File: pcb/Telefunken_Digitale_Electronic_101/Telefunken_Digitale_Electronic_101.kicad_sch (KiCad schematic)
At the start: 0 parts

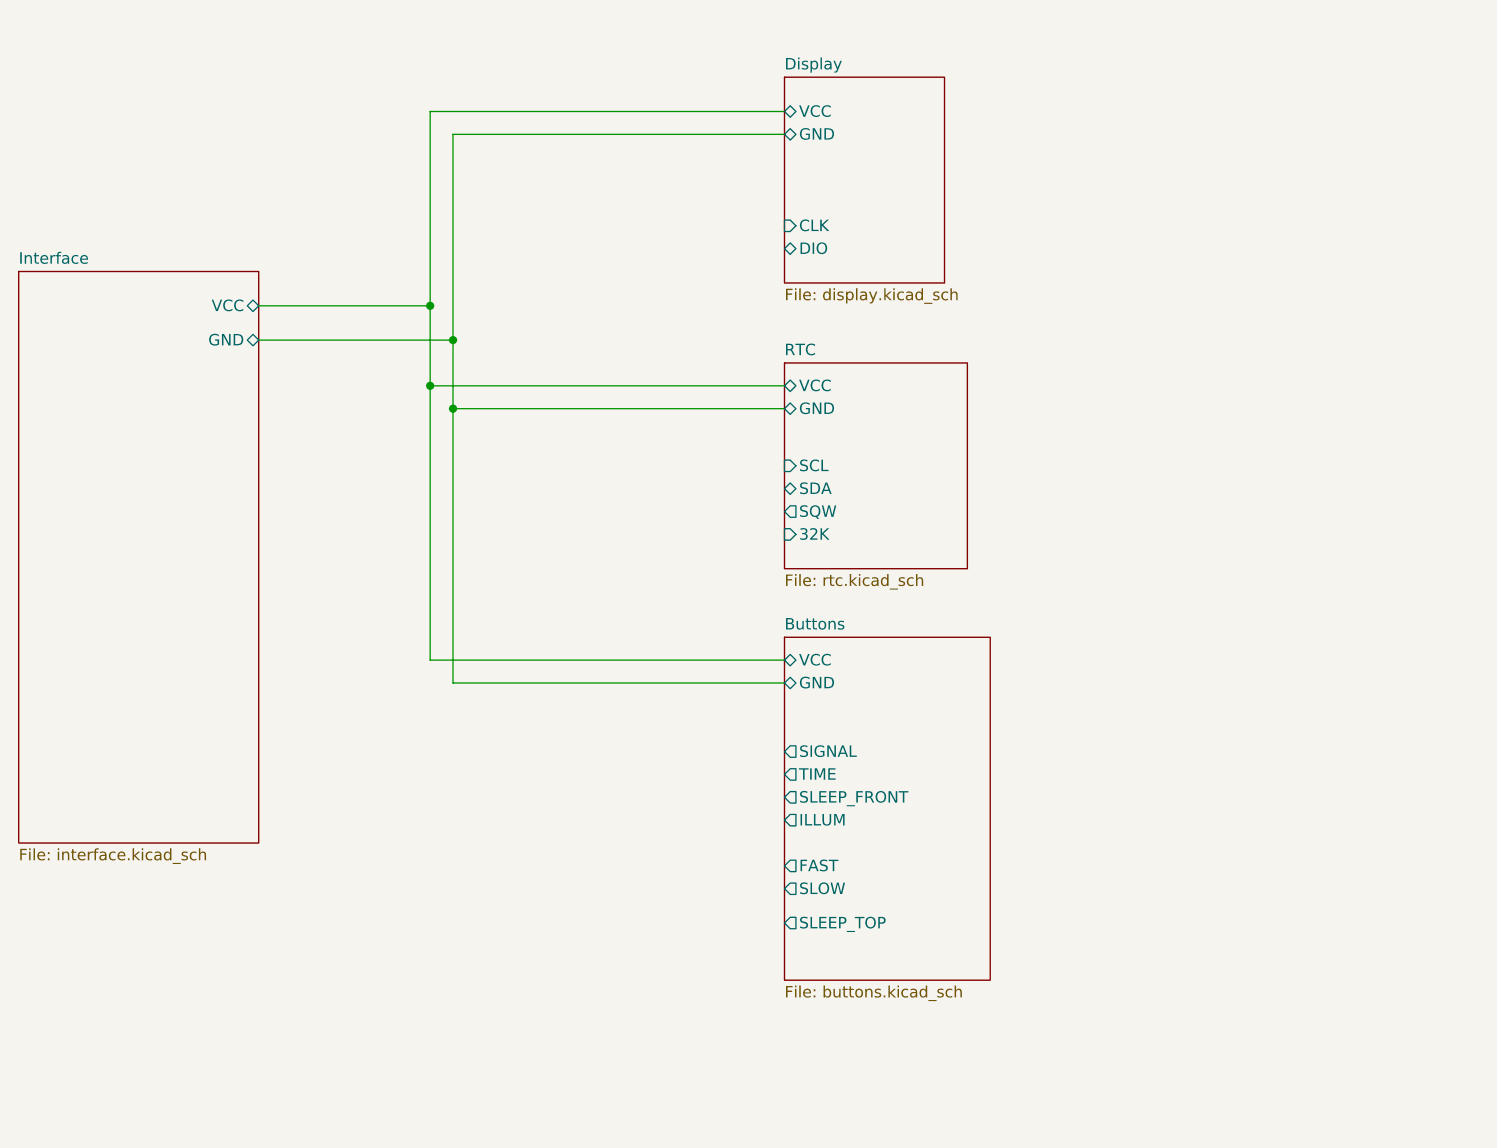
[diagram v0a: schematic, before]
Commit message: SCH - top level: connected everything
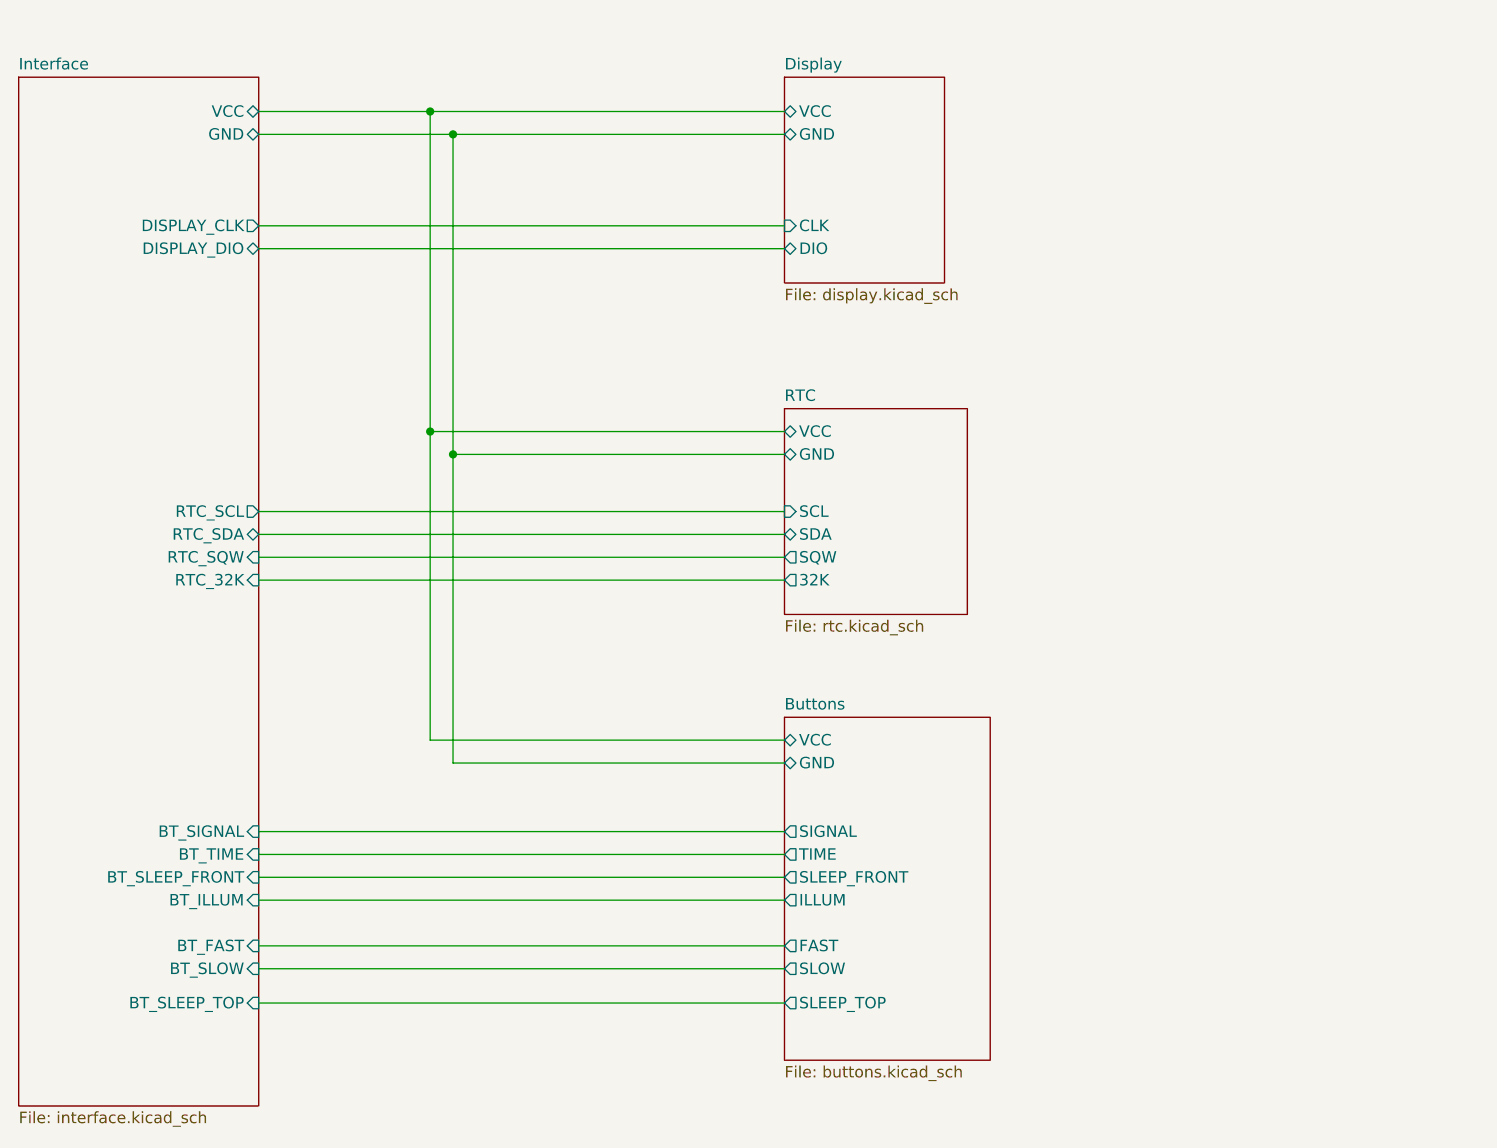
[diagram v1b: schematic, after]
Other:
- sheet Interface ports: added BT_FAST, BT_ILLUM, BT_SIGNAL, BT_SLEEP_FRONT, BT_SLEEP_TOP, BT_SLOW, BT_TIME, DISPLAY_CLK, DISPLAY_DIO, RTC_32K, RTC_SCL, RTC_SDA, RTC_SQW; removed none

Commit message: SCH - top level: reflect new button reading strategy
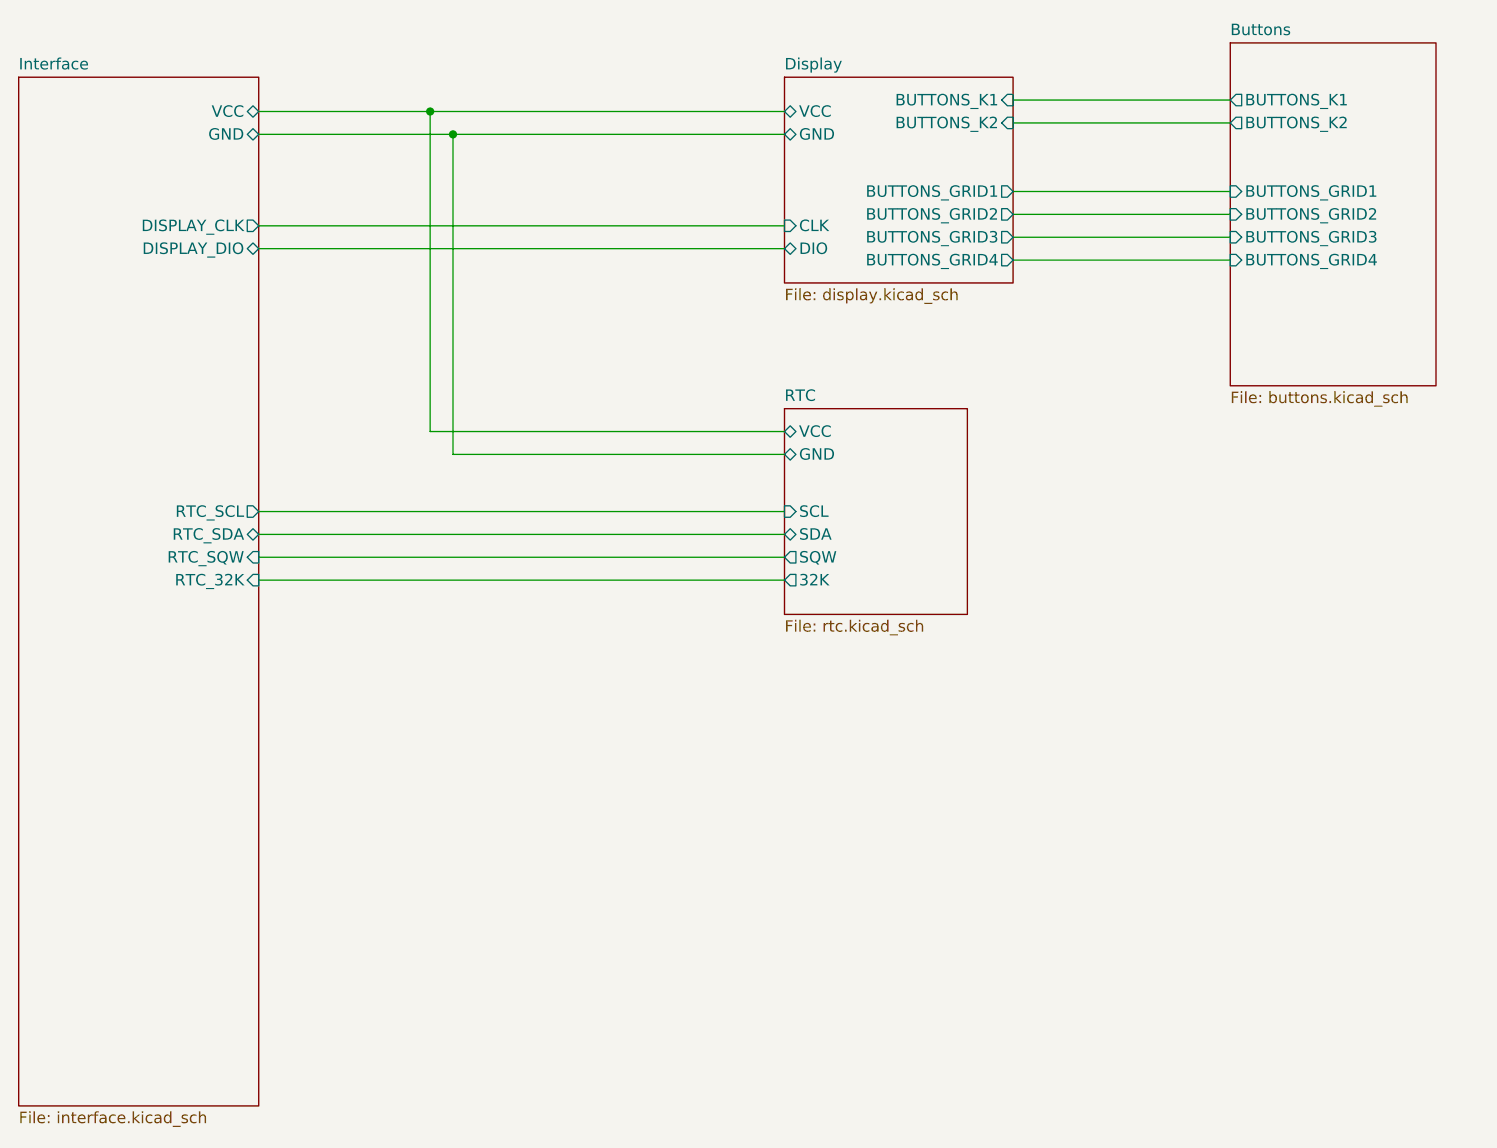
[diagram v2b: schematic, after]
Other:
- sheet Buttons ports: added BUTTONS_GRID1, BUTTONS_GRID2, BUTTONS_GRID3, BUTTONS_GRID4, BUTTONS_K1, BUTTONS_K2; removed FAST, GND, ILLUM, SIGNAL, SLEEP_FRONT, SLEEP_TOP, SLOW, TIME, VCC
- sheet Display ports: added BUTTONS_GRID1, BUTTONS_GRID2, BUTTONS_GRID3, BUTTONS_GRID4, BUTTONS_K1, BUTTONS_K2; removed none
- sheet Interface ports: added none; removed BT_FAST, BT_ILLUM, BT_SIGNAL, BT_SLEEP_FRONT, BT_SLEEP_TOP, BT_SLOW, BT_TIME

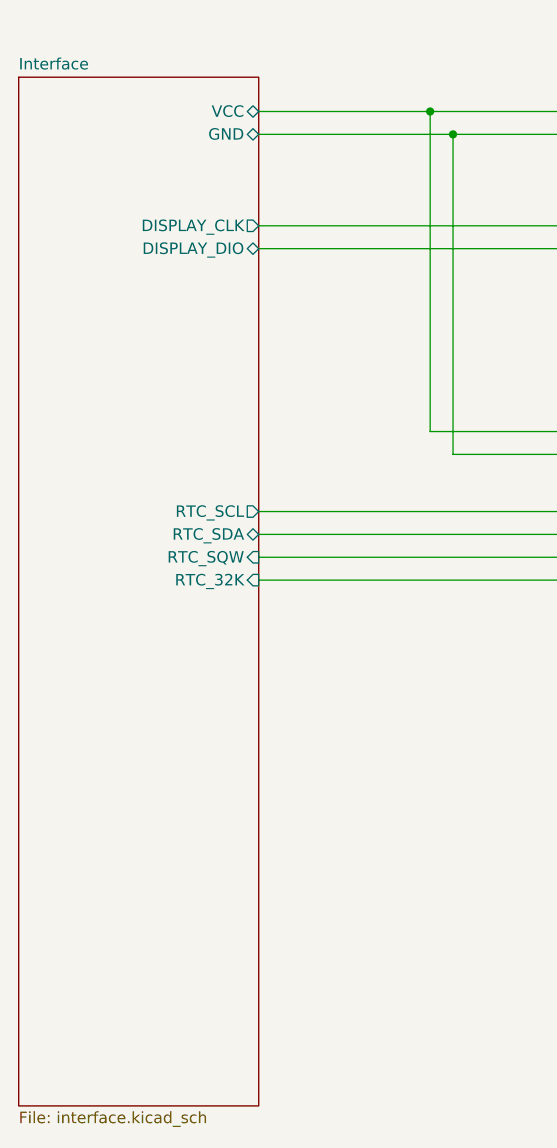
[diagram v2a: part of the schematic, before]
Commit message: SCH and PCB: added the Mounting Pads (a few chosen ones)
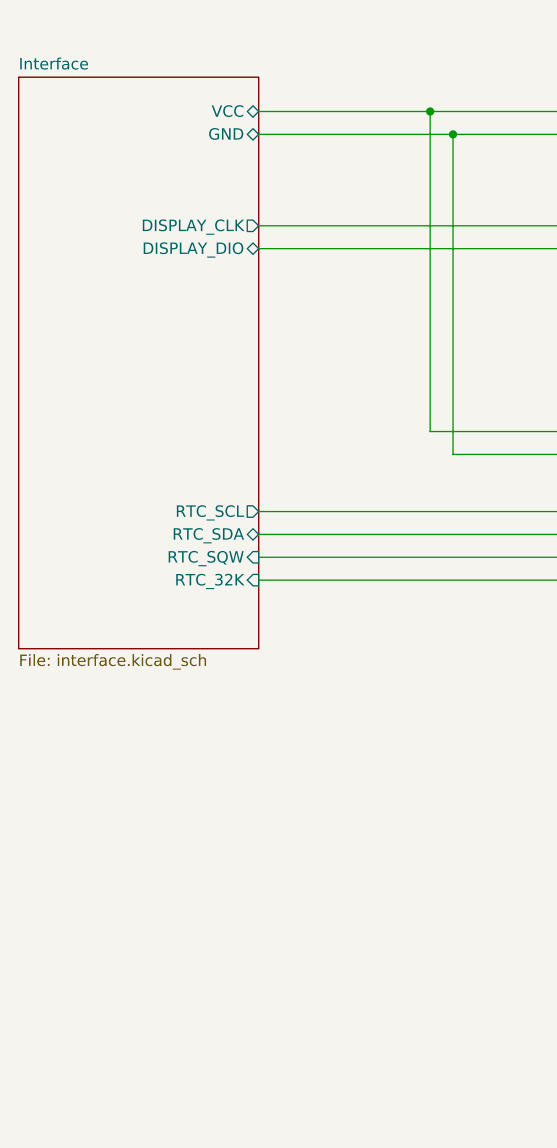
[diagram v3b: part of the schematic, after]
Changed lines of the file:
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@@
 	(sheet
 		(at 95.25 41.91)
-		(size 26.67 114.3)
+		(size 26.67 63.5)
 		(exclude_from_sim no)
 		(in_bom yes)
@@
 		)
 		(property "Sheetfile" "interface.kicad_sch"
-			(at 95.25 156.7946 0)
+			(at 95.25 105.9946 0)
 			(show_name no)
 			(do_not_autoplace no)
